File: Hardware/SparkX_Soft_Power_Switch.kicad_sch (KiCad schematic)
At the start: 38 parts, among them J1 JST_2mm_LiPo, J2 JST_2mm_LiPo, J3 Conn_01x06, Q1 BSS138, Q2 BSS138, SW1 SMD_5.2x5.2mm_h1.9mm, U2 74LVC1G14, U3 74LVC1G17, U4 74LVC1G175, U5 MIC94064YC6

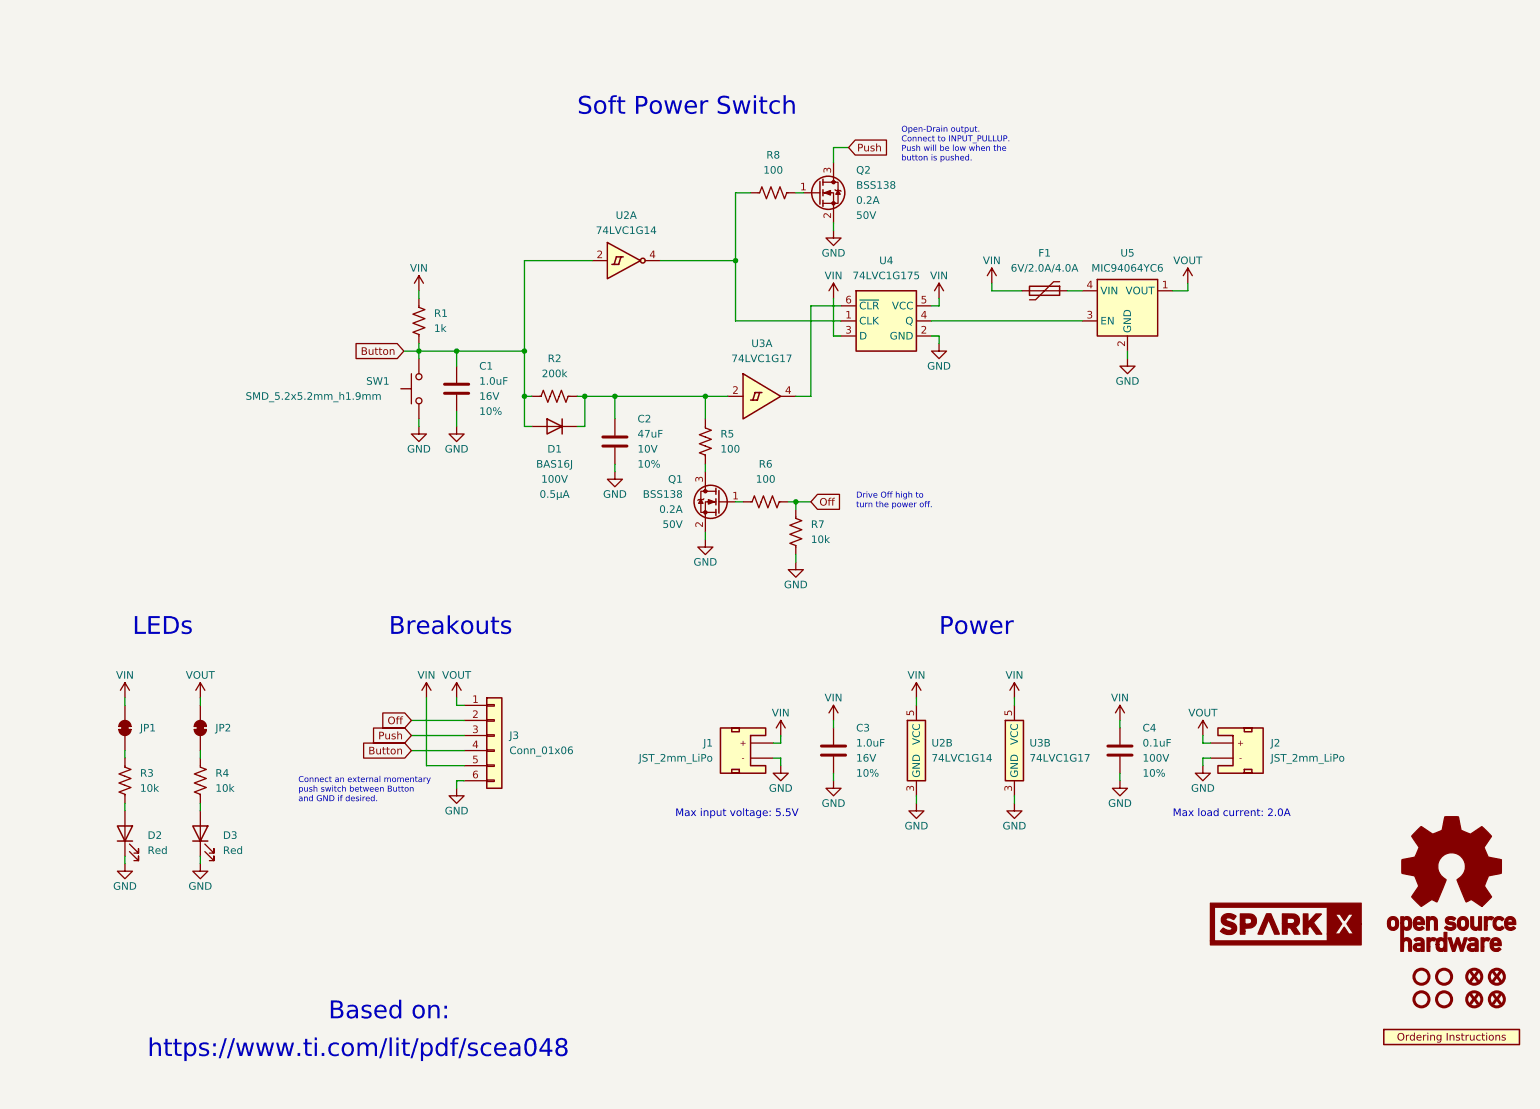
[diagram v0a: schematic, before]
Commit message: Change to SIL2308 - for battery charging
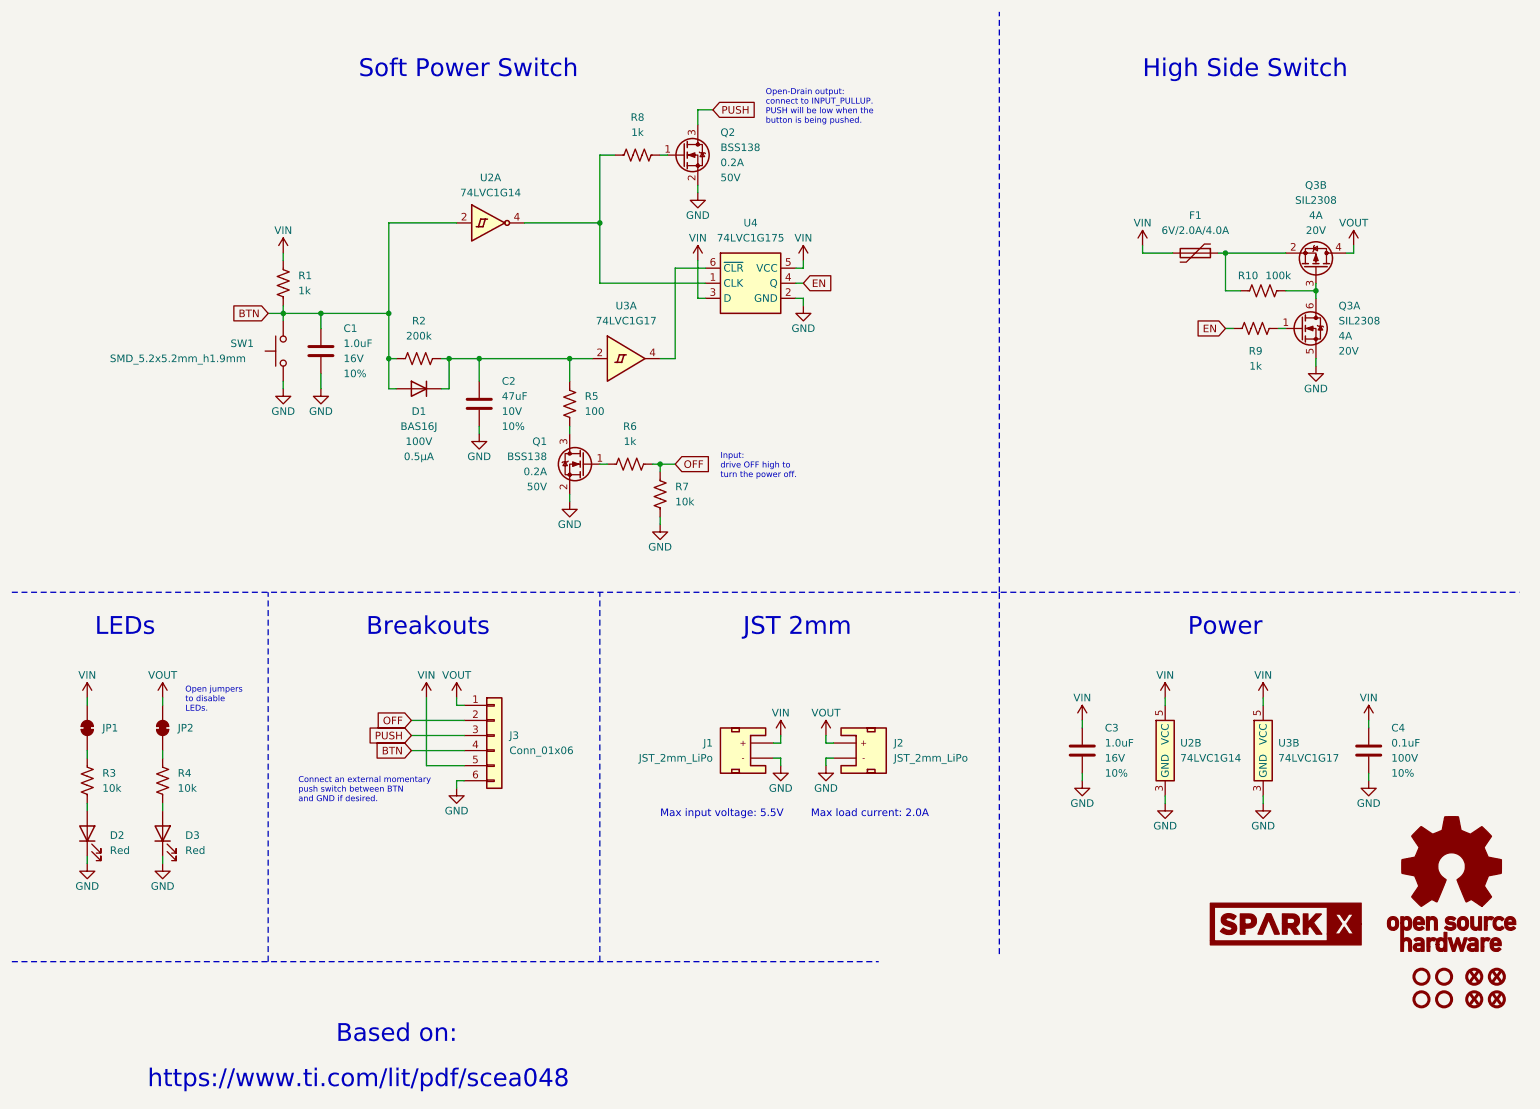
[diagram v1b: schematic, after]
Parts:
- removed R6, R8: 100, SparkFun-Resistor:R_0603_1608Metric, symbol SparkFun-Resistor:100_0603
- removed U1: ~, SparkFun-Aesthetic:Ordering_Instructions, symbol SparkFun-Aesthetic:Ordering_Instructions
- removed U5: MIC94064YC6, SparkFun-Semiconductor-Standard:SOT-323, symbol SparkFun-IC-Power:MIC94064YC6
- added Q3: SIL2308, SparkFun-Semiconductor-Standard:SOT23-6-Tight, symbol SparkFun-DiscreteSemi:Q_NPMOS_DUAL_4A_20V
- added R10: 100k, SparkFun-Resistor:R_0603_1608Metric, symbol SparkFun-Resistor:100k_0603
- added R6, R8, R9: 1k, SparkFun-Resistor:R_0603_1608Metric, symbol SparkFun-Resistor:1k_0603
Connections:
- net GND: now also Q3.5 (S)
- net VOUT: now also Q3.4 (D)
- net at Q2.1 (G): now also R8.2
- net at U2.4, U4.1 (CLK): now also R8.1
- net EN: now reaches U4.4 (Q)
- net EN: now also R9.2
- net at F1.1: now also Q3.2 (1), R10.2
- net at Q1.1 (G): now also R6.1
- net Button renamed BTN
- net BTN: now also SW1.2; no longer SW1.3
- net Off renamed OFF
- net OFF: now also R6.2
- net Push renamed PUSH
- new net: Q3.1 (G), R9.1
- new net: Q3.3 (G), Q3.6 (D), R10.1
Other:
- note added: "Connect an external momentary push switch between BTN and GND if desired."
- note added: "High Side Switch"
- note added: "Input: drive OFF high to turn the power off."
- note added: "JST 2mm"
- note added: "Open jumpers to disable LEDs."
- note added: "Open-Drain output: connect to INPUT_PULLUP. PUSH will be low when the button is being pushed."
- note removed: "Connect an external momentary push switch between Button and GND if desired."
- note removed: "Drive Off high to turn the power off."
- note removed: "Open-Drain output. Connect to INPUT_PULLUP. Push will be low when the button is pushed."
- title: SparkX Soft Power Switch -> SparkX Soft Power Switch Mk2
- moved on the sheet: C1, C2, C3, C4, D1, D2, D3, F1, J2, JP1, JP2, Q1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

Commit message: Add PROD_IDs
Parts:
- U2: PROD_ID IC- -> IC-21903
- U3: PROD_ID IC- -> IC-21904
- U4: PROD_ID IC- -> IC-21905
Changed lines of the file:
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@@
       (effects (font (size 1.27 1.27)) hide)
     )
-    (property "PROD_ID" "IC-" (at 137.16 72.39 0)
+    (property "PROD_ID" "IC-21905" (at 137.16 72.39 0)
       (effects (font (size 1.27 1.27)) hide)
     )
@@
       (effects (font (size 1.27 1.27)) hide)
     )
-    (property "PROD_ID" "IC-" (at 207.01 153.67 0)
+    (property "PROD_ID" "IC-21903" (at 207.01 153.67 0)
       (effects (font (size 1.27 1.27)) hide)
     )
@@
       (effects (font (size 1.27 1.27)) hide)
     )
-    (property "PROD_ID" "IC-" (at 223.52 153.67 0)
+    (property "PROD_ID" "IC-21904" (at 223.52 153.67 0)
       (effects (font (size 1.27 1.27)) hide)
     )
@@
       (effects (font (size 1.27 1.27)) hide)
     )
-    (property "PROD_ID" "IC-" (at 93.98 64.77 0)
+    (property "PROD_ID" "IC-21903" (at 93.98 64.77 0)
       (effects (font (size 1.27 1.27)) hide)
     )
@@
       (effects (font (size 1.27 1.27)) hide)
     )
-    (property "PROD_ID" "IC-" (at 116.84 87.63 0)
-      (effects (font (size 1.27 1.27)) hide)
-    )
+    (property "PROD_ID" "IC-21904" (at 116.84 87.63 0)
+      (effects (font (size 1.27 1.27)) hide)
+    )

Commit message: Update 100R resistor PROD_ID
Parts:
- R5: PROD_ID RES-07836 -> RES-07863
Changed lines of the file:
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@@
       (effects (font (size 1.27 1.27)) hide)
     )
-    (property "PROD_ID" "RES-07836" (at 113.538 78.74 0)
+    (property "PROD_ID" "RES-07863" (at 113.538 78.74 0)
       (effects (font (size 1.27 1.27)) hide)
     )

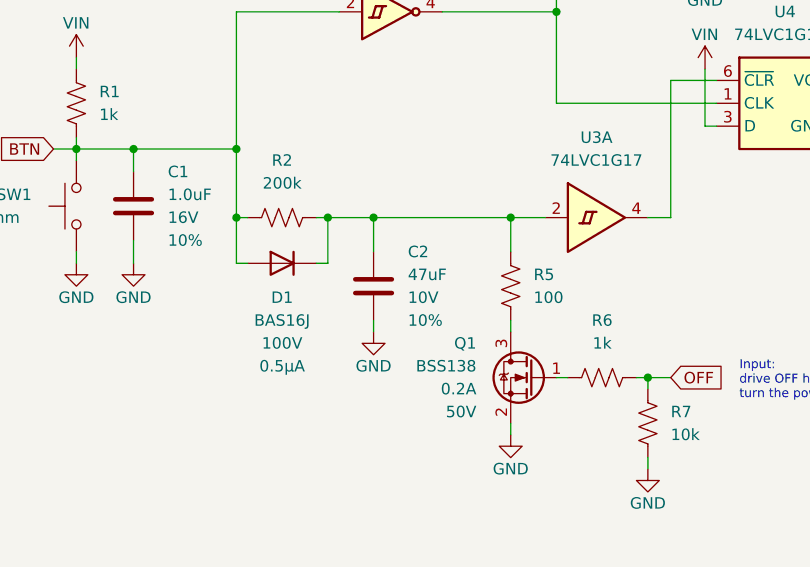
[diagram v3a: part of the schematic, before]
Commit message: Update to KiCad 8. Update 47uF cap
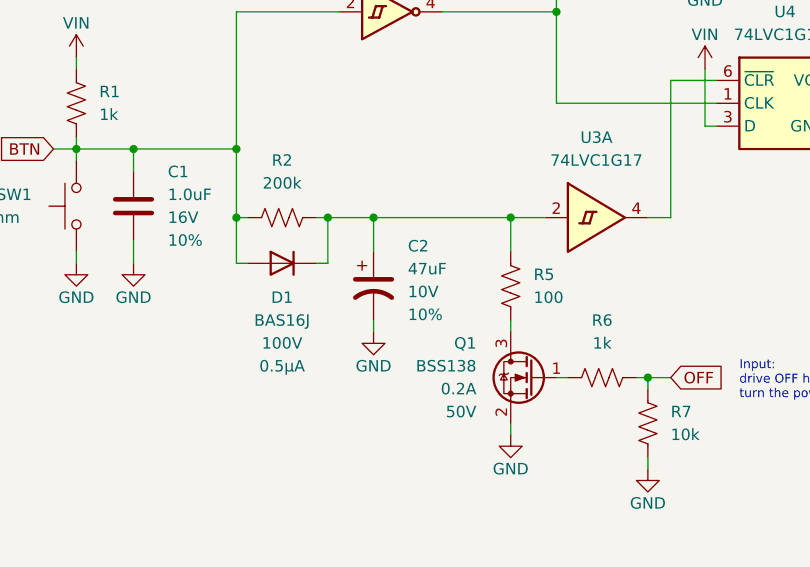
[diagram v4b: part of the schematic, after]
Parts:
- removed C2: 47uF, SparkFun-Capacitor:C_1210_3225Metric, symbol SparkFun-Capacitor:47uF_0805_10V_20%_1
- added C2: 47uF, SparkFun-Capacitor:EIA-3528, symbol SparkFun-Capacitor:47uF_3528_10V_10%
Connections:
- net GND: now also C2.2
- net at D1.C, R2.1, R5.1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: now also C2.1

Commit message: Update 3D models
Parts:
- D2, D3: footprint SparkFun-LED:LED_0603_1608Metric -> SparkFun-LED:LED_0603_1608Metric_Red
- SW1: footprint SparkFun-Switch:Push_SMD_5.2x5.2mm -> SparkFun-Switch:Push_SMD_5.2x5.2mm_h1.9mm
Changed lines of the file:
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@@
 			)
 		)
-		(property "Footprint" "SparkFun-LED:LED_0603_1608Metric"
+		(property "Footprint" "SparkFun-LED:LED_0603_1608Metric_Red"
 			(at 44.45 151.13 0)
 			(effects
@@
 			)
 		)
-		(property "Footprint" "SparkFun-Switch:Push_SMD_5.2x5.2mm"
+		(property "Footprint" "SparkFun-Switch:Push_SMD_5.2x5.2mm_h1.9mm"
 			(at 63.5 69.85 0)
 			(effects
@@
 			)
 		)
-		(property "Footprint" "SparkFun-LED:LED_0603_1608Metric"
+		(property "Footprint" "SparkFun-LED:LED_0603_1608Metric_Red"
 			(at 31.75 151.13 0)
 			(effects
